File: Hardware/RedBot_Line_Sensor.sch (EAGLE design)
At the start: 9 parts, among them U1 QRE1113

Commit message: Change to Rev 10 for release  - flipped connector to bottom side of board  - change revision number
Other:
- note added: "10"
- note removed: "v01"
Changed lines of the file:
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@@
 <plain>
 <text x="172.72" y="7.62" size="3.81" layer="94">M. Hord</text>
-<text x="237.49" y="6.604" size="3.81" layer="94">v01</text>
+<text x="237.49" y="6.604" size="3.81" layer="94">10</text>
 </plain>
 <instances>

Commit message: Production Readied
Added fiducial reference points & created panel for manufacture.
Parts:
- added FID1, FID2: FIDUCIALUFIDUCIAL, SparkFun-Aesthetics:FIDUCIALUFIDUCIAL
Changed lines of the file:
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@@
 <part name="STANDOFF1" library="SparkFun-Electromechanical" deviceset="STAND-OFF" device=""/>
 <part name="LOGO3" library="SparkFun-Aesthetics" deviceset="LOGO-SFE" device="SK"/>
+<part name="FID1" library="SparkFun-Aesthetics" deviceset="FIDUCIAL" device="UFIDUCIAL"/>
+<part name="FID2" library="SparkFun-Aesthetics" deviceset="FIDUCIAL" device="UFIDUCIAL"/>
 </parts>
 <sheets>
@@
 <instance part="STANDOFF1" gate="G$1" x="246.38" y="33.02"/>
 <instance part="LOGO3" gate="G$1" x="241.3" y="17.78"/>
+<instance part="FID1" gate="G$1" x="241.3" y="30.48"/>
+<instance part="FID2" gate="G$1" x="241.3" y="25.4"/>
 </instances>
 <busses>

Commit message: QC Revision
Changes:
1.) 0402 to 0603 footprint
2.) Updated QRE1113 footprint
3.) New 3-pin SMD header footprint w/ bosses
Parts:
- JP1: device SparkFun-Connectors:M03SMD_RA_MALE -> SparkFun-Connectors:M03SMD_RA_MALE_POST
- R2: device SparkFun-Resistors:10KOHM1/10W1%(0603) -> SparkFun-Resistors:10KOHM1/10W1%(0603)0603
- U1: value QRE1113 -> QRE1113SMD-W; device SparkFun-Sensors:QRE1113 -> SparkFun-Sensors:QRE1113SMD-W
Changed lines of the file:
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@@
 <?xml version="1.0" encoding="utf-8"?>
 <!DOCTYPE eagle SYSTEM "eagle.dtd">
-<eagle version="6.4">
+<eagle version="6.5.0">
 <drawing>
 <settings>
@@
 <grid distance="0.1" unitdist="inch" unit="inch" style="lines" multiple="1" display="no" altdistance="0.01" altunitdist="inch" altunit="inch"/>
 <layers>
-<layer number="1" name="Top" color="4" fill="1" visible="no" active="no"/>
-<layer number="2" name="Route2" color="1" fill="3" visible="no" active="no"/>
-<layer number="3" name="Route3" color="4" fill="3" visible="no" active="no"/>
-<layer number="4" name="Route4" color="1" fill="4" visible="no" active="no"/>
-<layer number="5" name="Route5" color="4" fill="4" visible="no" active="no"/>
-<layer number="6" name="Route6" color="1" fill="8" visible="no" active="no"/>
-<layer number="7" name="Route7" color="4" fill="8" visible="no" active="no"/>
-<layer number="8" name="Route8" color="1" fill="2" visible="no" active="no"/>
-<layer number="9" name="Route9" color="4" fill="2" visible="no" active="no"/>
-<layer number="10" name="Route10" color="1" fill="7" visible="no" active="no"/>
-<layer number="11" name="Route11" color="4" fill="7" visible="no" active="no"/>
-<layer number="12" name="Route12" color="1" fill="5" visible="no" active="no"/>
-<layer number="13" name="Route13" color="4" fill="5" visible="no" active="no"/>
-<layer number="14" name="Route14" color="1" fill="6" visible="no" active="no"/>
-<layer number="15" name="Route15" color="4" fill="6" visible="no" active="no"/>
-<layer number="16" name="Bottom" color="1" fill="1" visible="no" active="no"/>
-<layer number="17" name="Pads" color="2" fill="1" visible="no" active="no"/>
-<layer number="18" name="Vias" color="2" fill="1" visible="no" active="no"/>
-<layer number="19" name="Unrouted" color="6" fill="1" visible="no" active="no"/>
-<layer number="20" name="Dimension" color="15" fill="1" visible="no" active="no"/>
-<layer number="21" name="tPlace" color="7" fill="1" visible="no" active="no"/>
-<layer number="22" name="bPlace" color="7" fill="1" visible="no" active="no"/>
-<layer number="23" name="tOrigins" color="15" fill="1" visible="no" active="no"/>
-<layer number="24" name="bOrigins" color="15" fill="1" visible="no" active="no"/>
-<layer number="25" name="tNames" color="7" fill="1" visible="no" active="no"/>
-<layer number="26" name="bNames" color="7" fill="1" visible="no" active="no"/>
-<layer number="27" name="tValues" color="7" fill="1" visible="no" active="no"/>
-<layer number="28" name="bValues" color="7" fill="1" visible="no" active="no"/>
+<layer number="1" name="Top" color="4" fill="1" visible="yes" active="no"/>
+<layer number="2" name="Route2" color="1" fill="3" visible="yes" active="no"/>
+<layer number="3" name="Route3" color="4" fill="3" visible="yes" active="no"/>
+<layer number="4" name="Route4" color="1" fill="4" visible="yes" active="no"/>
+<layer number="5" name="Route5" color="4" fill="4" visible="yes" active="no"/>
+<layer number="6" name="Route6" color="1" fill="8" visible="yes" active="no"/>
+<layer number="7" name="Route7" color="4" fill="8" visible="yes" active="no"/>
+<layer number="8" name="Route8" color="1" fill="2" visible="yes" active="no"/>
+<layer number="9" name="Route9" color="4" fill="2" visible="yes" active="no"/>
+<layer number="10" name="Route10" color="1" fill="7" visible="yes" active="no"/>
+<layer number="11" name="Route11" color="4" fill="7" visible="yes" active="no"/>
+<layer number="12" name="Route12" color="1" fill="5" visible="yes" active="no"/>
+<layer number="13" name="Route13" color="4" fill="5" visible="yes" active="no"/>
+<layer number="14" name="Route14" color="1" fill="6" visible="yes" active="no"/>
+<layer number="15" name="Route15" color="4" fill="6" visible="yes" active="no"/>
+<layer number="16" name="Bottom" color="1" fill="1" visible="yes" active="no"/>
+<layer number="17" name="Pads" color="2" fill="1" visible="yes" active="no"/>
+<layer number="18" name="Vias" color="2" fill="1" visible="yes" active="no"/>
+<layer number="19" name="Unrouted" color="6" fill="1" visible="yes" active="no"/>
+<layer number="20" name="Dimension" color="6" fill="1" visible="yes" active="no"/>
+<layer number="21" name="tPlace" color="16" fill="1" visible="yes" active="no"/>
+<layer number="22" name="bPlace" color="14" fill="1" visible="yes" active="no"/>
+<layer number="23" name="tOrigins" color="15" fill="1" visible="yes" active="no"/>
+<layer number="24" name="bOrigins" color="15" fill="1" visible="yes" active="no"/>
+<layer number="25" name="tNames" color="7" fill="1" visible="yes" active="no"/>
+<layer number="26" name="bNames" color="7" fill="1" visible="yes" active="no"/>
+<layer number="27" name="tValues" color="7" fill="1" visible="yes" active="no"/>
+<layer number="28" name="bValues" color="7" fill="1" visible="yes" active="no"/>
 <layer number="29" name="tStop" color="7" fill="3" visible="no" active="no"/>
 <layer number="30" name="bStop" color="7" fill="6" visible="no" active="no"/>
@@
 <layer number="35" name="tGlue" color="7" fill="4" visible="no" active="no"/>
 <layer number="36" name="bGlue" color="7" fill="5" visible="no" active="no"/>
-<layer number="37" name="tTest" color="7" fill="1" visible="no" active="no"/>
-<layer number="38" name="bTest" color="7" fill="1" visible="no" active="no"/>
+<layer number="37" name="tTest" color="7" fill="1" visible="yes" active="no"/>
+<layer number="38" name="bTest" color="7" fill="1" visible="yes" active="no"/>
 <layer number="39" name="tKeepout" color="4" fill="11" visible="no" active="no"/>
 <layer number="40" name="bKeepout" color="1" fill="11" visible="no" active="no"/>
@@
 <layer number="44" name="Drills" color="7" fill="1" visible="no" active="no"/>
 <layer number="45" name="Holes" color="7" fill="1" visible="no" active="no"/>
-<layer number="46" name="Milling" color="3" fill="1" visible="no" active="no"/>
-<layer number="47" name="Measures" color="7" fill="1" visible="no" active="no"/>
-<layer number="48" name="Document" color="7" fill="1" visible="no" active="no"/>
-<layer number="49" name="Reference" color="7" fill="1" visible="no" active="no"/>
-<layer number="50" name="dxf" color="7" fill="1" visible="no" active="no"/>
-<layer number="51" name="tDocu" color="7" fill="1" visible="no" active="no"/>
-<layer number="52" name="bDocu" color="7" fill="1" visible="no" active="no"/>
-<layer number="53" name="tGND_GNDA" color="7" fill="9" visible="no" active="no"/>
-<layer number="54" name="bGND_GNDA" color="1" fill="9" visible="no" active="no"/>
-<layer number="56" name="wert" color="7" fill="1" visible="no" active="no"/>
+<layer number="46" name="Milling" color="3" fill="1" visible="yes" active="no"/>
+<layer number="47" name="Measures" color="7" fill="1" visible="yes" active="no"/>
+<layer number="48" name="Document" color="7" fill="1" visible="yes" active="no"/>
+<layer number="49" name="Reference" color="7" fill="1" visible="yes" active="no"/>
+<layer number="50" name="dxf" color="7" fill="1" visible="yes" active="no"/>
+<layer number="51" name="tDocu" color="6" fill="1" visible="yes" active="no"/>
+<layer number="52" name="bDocu" color="7" fill="1" visible="yes" active="no"/>
+<layer number="53" name="tGND_GNDA" color="7" fill="9" visible="yes" active="no"/>
+<layer number="54" name="bGND_GNDA" color="1" fill="9" visible="yes" active="no"/>
+<layer number="56" name="wert" color="7" fill="1" visible="yes" active="no"/>
 <layer number="91" name="Nets" color="2" fill="1" visible="yes" active="yes"/>
 <layer number="92" name="Busses" color="1" fill="1" visible="yes" active="yes"/>
@@
 <layer number="106" name="bPlate" color="7" fill="1" visible="no" active="yes"/>
 <layer number="107" name="Crop" color="7" fill="1" visible="no" active="yes"/>
+<layer number="108" name="tplace-old" color="10" fill="1" visible="yes" active="yes"/>
+<layer number="109" name="ref-old" color="11" fill="1" visible="yes" active="yes"/>
 <layer number="116" name="Patch_BOT" color="9" fill="4" visible="no" active="yes"/>
 <layer number="121" name="_tsilk" color="7" fill="1" visible="no" active="yes"/>
@@
 <part name="LOGO1" library="SparkFun-Aesthetics" deviceset="LOGO-SFE" device="SK"/>
 <part name="LOGO2" library="SparkFun-Aesthetics" deviceset="OSHW-LOGO" device="S"/>
-<part name="U1" library="SparkFun-Sensors" deviceset="QRE1113" device=""/>
+<part name="U1" library="SparkFun-Sensors" deviceset="QRE1113" device="SMD-W" value="QRE1113SMD-W"/>
 <part name="R1" library="SparkFun-Resistors" deviceset="100-1%" device="" value="100"/>
-<part name="R2" library="SparkFun-Resistors" deviceset="10KOHM1/10W1%(0603)" device="" value="10k"/>
-<part name="JP1" library="SparkFun-Connectors" deviceset="M03" device="SMD_RA_MALE"/>
+<part name="R2" library="SparkFun-Resistors" deviceset="10KOHM1/10W1%(0603)" device="0603" value="10k"/>
+<part name="JP1" library="SparkFun-Connectors" deviceset="M03" device="SMD_RA_MALE_POST"/>
 <part name="STANDOFF1" library="SparkFun-Electromechanical" deviceset="STAND-OFF" device=""/>
 <part name="LOGO3" library="SparkFun-Aesthetics" deviceset="LOGO-SFE" device="SK"/>

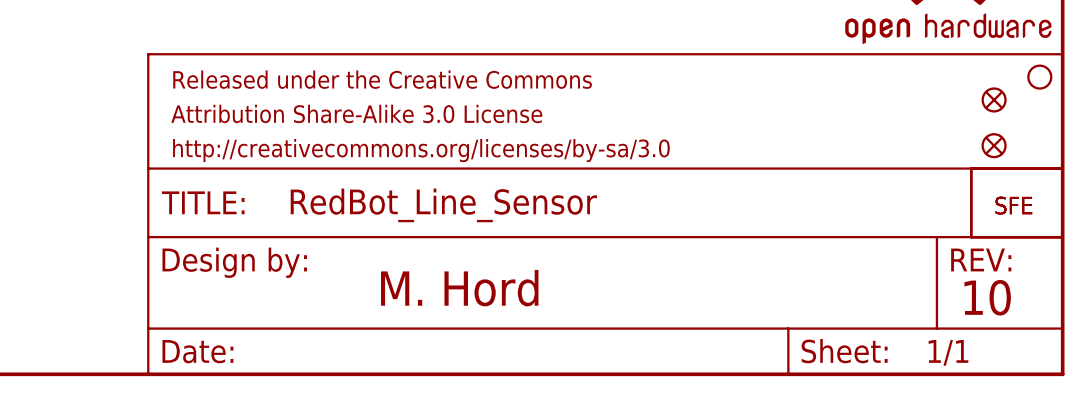
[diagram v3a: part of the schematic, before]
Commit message: Minor aesthetic fixes
1.) Moved VCC via away from silk
2.) Moved board name silk away from header boss holes
3.) Updated version info in schematic.
4.) Moved flame on top side out to avoid resistor tcreme.
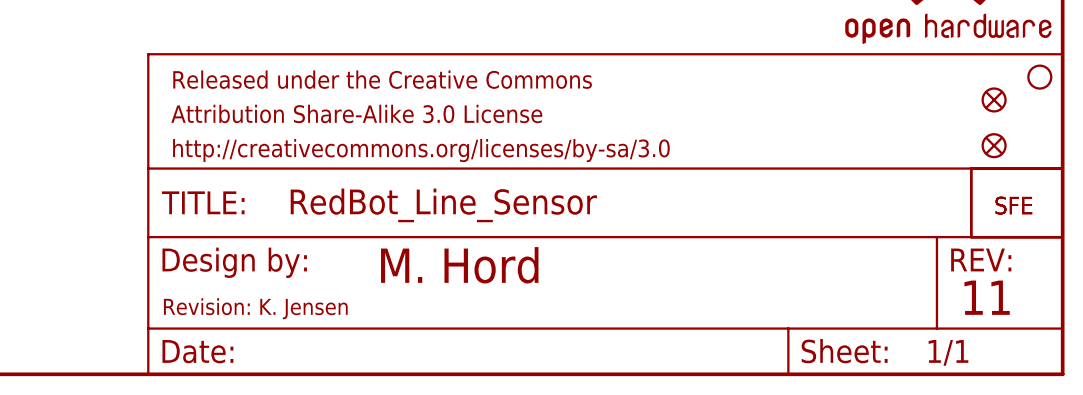
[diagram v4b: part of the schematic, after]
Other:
- note added: "11"
- note added: "Revision: K. Jensen"
- note removed: "10"
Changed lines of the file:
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@@
 <?xml version="1.0" encoding="utf-8"?>
 <!DOCTYPE eagle SYSTEM "eagle.dtd">
-<eagle version="6.5.0">
+<eagle version="6.4">
 <drawing>
 <settings>
@@
 <grid distance="0.1" unitdist="inch" unit="inch" style="lines" multiple="1" display="no" altdistance="0.01" altunitdist="inch" altunit="inch"/>
 <layers>
-<layer number="1" name="Top" color="4" fill="1" visible="yes" active="no"/>
-<layer number="2" name="Route2" color="1" fill="3" visible="yes" active="no"/>
-<layer number="3" name="Route3" color="4" fill="3" visible="yes" active="no"/>
-<layer number="4" name="Route4" color="1" fill="4" visible="yes" active="no"/>
-<layer number="5" name="Route5" color="4" fill="4" visible="yes" active="no"/>
-<layer number="6" name="Route6" color="1" fill="8" visible="yes" active="no"/>
-<layer number="7" name="Route7" color="4" fill="8" visible="yes" active="no"/>
-<layer number="8" name="Route8" color="1" fill="2" visible="yes" active="no"/>
-<layer number="9" name="Route9" color="4" fill="2" visible="yes" active="no"/>
-<layer number="10" name="Route10" color="1" fill="7" visible="yes" active="no"/>
-<layer number="11" name="Route11" color="4" fill="7" visible="yes" active="no"/>
-<layer number="12" name="Route12" color="1" fill="5" visible="yes" active="no"/>
-<layer number="13" name="Route13" color="4" fill="5" visible="yes" active="no"/>
-<layer number="14" name="Route14" color="1" fill="6" visible="yes" active="no"/>
-<layer number="15" name="Route15" color="4" fill="6" visible="yes" active="no"/>
-<layer number="16" name="Bottom" color="1" fill="1" visible="yes" active="no"/>
-<layer number="17" name="Pads" color="2" fill="1" visible="yes" active="no"/>
-<layer number="18" name="Vias" color="2" fill="1" visible="yes" active="no"/>
-<layer number="19" name="Unrouted" color="6" fill="1" visible="yes" active="no"/>
-<layer number="20" name="Dimension" color="6" fill="1" visible="yes" active="no"/>
-<layer number="21" name="tPlace" color="16" fill="1" visible="yes" active="no"/>
-<layer number="22" name="bPlace" color="14" fill="1" visible="yes" active="no"/>
-<layer number="23" name="tOrigins" color="15" fill="1" visible="yes" active="no"/>
-<layer number="24" name="bOrigins" color="15" fill="1" visible="yes" active="no"/>
-<layer number="25" name="tNames" color="7" fill="1" visible="yes" active="no"/>
-<layer number="26" name="bNames" color="7" fill="1" visible="yes" active="no"/>
-<layer number="27" name="tValues" color="7" fill="1" visible="yes" active="no"/>
-<layer number="28" name="bValues" color="7" fill="1" visible="yes" active="no"/>
+<layer number="1" name="Top" color="4" fill="1" visible="no" active="no"/>
+<layer number="2" name="Route2" color="1" fill="3" visible="no" active="no"/>
+<layer number="3" name="Route3" color="4" fill="3" visible="no" active="no"/>
+<layer number="4" name="Route4" color="1" fill="4" visible="no" active="no"/>
+<layer number="5" name="Route5" color="4" fill="4" visible="no" active="no"/>
+<layer number="6" name="Route6" color="1" fill="8" visible="no" active="no"/>
+<layer number="7" name="Route7" color="4" fill="8" visible="no" active="no"/>
+<layer number="8" name="Route8" color="1" fill="2" visible="no" active="no"/>
+<layer number="9" name="Route9" color="4" fill="2" visible="no" active="no"/>
+<layer number="10" name="Route10" color="1" fill="7" visible="no" active="no"/>
+<layer number="11" name="Route11" color="4" fill="7" visible="no" active="no"/>
+<layer number="12" name="Route12" color="1" fill="5" visible="no" active="no"/>
+<layer number="13" name="Route13" color="4" fill="5" visible="no" active="no"/>
+<layer number="14" name="Route14" color="1" fill="6" visible="no" active="no"/>
+<layer number="15" name="Route15" color="4" fill="6" visible="no" active="no"/>
+<layer number="16" name="Bottom" color="1" fill="1" visible="no" active="no"/>
+<layer number="17" name="Pads" color="2" fill="1" visible="no" active="no"/>
+<layer number="18" name="Vias" color="2" fill="1" visible="no" active="no"/>
+<layer number="19" name="Unrouted" color="6" fill="1" visible="no" active="no"/>
+<layer number="20" name="Dimension" color="6" fill="1" visible="no" active="no"/>
+<layer number="21" name="tPlace" color="16" fill="1" visible="no" active="no"/>
+<layer number="22" name="bPlace" color="14" fill="1" visible="no" active="no"/>
+<layer number="23" name="tOrigins" color="15" fill="1" visible="no" active="no"/>
+<layer number="24" name="bOrigins" color="15" fill="1" visible="no" active="no"/>
+<layer number="25" name="tNames" color="7" fill="1" visible="no" active="no"/>
+<layer number="26" name="bNames" color="7" fill="1" visible="no" active="no"/>
+<layer number="27" name="tValues" color="7" fill="1" visible="no" active="no"/>
+<layer number="28" name="bValues" color="7" fill="1" visible="no" active="no"/>
 <layer number="29" name="tStop" color="7" fill="3" visible="no" active="no"/>
 <layer number="30" name="bStop" color="7" fill="6" visible="no" active="no"/>
@@
 <layer number="35" name="tGlue" color="7" fill="4" visible="no" active="no"/>
 <layer number="36" name="bGlue" color="7" fill="5" visible="no" active="no"/>
-<layer number="37" name="tTest" color="7" fill="1" visible="yes" active="no"/>
-<layer number="38" name="bTest" color="7" fill="1" visible="yes" active="no"/>
+<layer number="37" name="tTest" color="7" fill="1" visible="no" active="no"/>
+<layer number="38" name="bTest" color="7" fill="1" visible="no" active="no"/>
 <layer number="39" name="tKeepout" color="4" fill="11" visible="no" active="no"/>
 <layer number="40" name="bKeepout" color="1" fill="11" visible="no" active="no"/>
@@
 <layer number="44" name="Drills" color="7" fill="1" visible="no" active="no"/>
 <layer number="45" name="Holes" color="7" fill="1" visible="no" active="no"/>
-<layer number="46" name="Milling" color="3" fill="1" visible="yes" active="no"/>
-<layer number="47" name="Measures" color="7" fill="1" visible="yes" active="no"/>
-<layer number="48" name="Document" color="7" fill="1" visible="yes" active="no"/>
-<layer number="49" name="Reference" color="7" fill="1" visible="yes" active="no"/>
-<layer number="50" name="dxf" color="7" fill="1" visible="yes" active="no"/>
-<layer number="51" name="tDocu" color="6" fill="1" visible="yes" active="no"/>
-<layer number="52" name="bDocu" color="7" fill="1" visible="yes" active="no"/>
-<layer number="53" name="tGND_GNDA" color="7" fill="9" visible="yes" active="no"/>
-<layer number="54" name="bGND_GNDA" color="1" fill="9" visible="yes" active="no"/>
-<layer number="56" name="wert" color="7" fill="1" visible="yes" active="no"/>
+<layer number="46" name="Milling" color="3" fill="1" visible="no" active="no"/>
+<layer number="47" name="Measures" color="7" fill="1" visible="no" active="no"/>
+<layer number="48" name="Document" color="7" fill="1" visible="no" active="no"/>
+<layer number="49" name="Reference" color="7" fill="1" visible="no" active="no"/>
+<layer number="50" name="dxf" color="7" fill="1" visible="no" active="no"/>
+<layer number="51" name="tDocu" color="6" fill="1" visible="no" active="no"/>
+<layer number="52" name="bDocu" color="7" fill="1" visible="no" active="no"/>
+<layer number="53" name="tGND_GNDA" color="7" fill="9" visible="no" active="no"/>
+<layer number="54" name="bGND_GNDA" color="1" fill="9" visible="no" active="no"/>
+<layer number="56" name="wert" color="7" fill="1" visible="no" active="no"/>
 <layer number="91" name="Nets" color="2" fill="1" visible="yes" active="yes"/>
 <layer number="92" name="Busses" color="1" fill="1" visible="yes" active="yes"/>
@@
 <sheet>
 <plain>
-<text x="172.72" y="7.62" size="3.81" layer="94">M. Hord</text>
-<text x="237.49" y="6.604" size="3.81" layer="94">10</text>
+<text x="172.72" y="10.16" size="3.81" layer="94">M. Hord</text>
+<text x="237.49" y="6.604" size="3.81" layer="94">11</text>
+<text x="148.844" y="6.604" size="1.778" layer="94">Revision: K. Jensen</text>
 </plain>
 <instances>

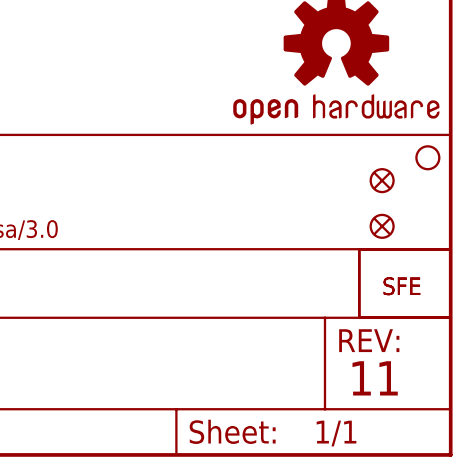
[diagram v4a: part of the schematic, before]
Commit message: Silk fixes and trace reroutes
Fixed top silk so pin labels are closer to edge of board and nothing
gets cut off. Removed flame from top. Cleaned up "out" and "vcc" traces
to be more efficient.
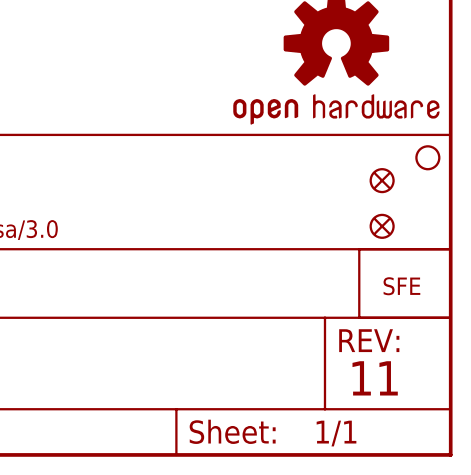
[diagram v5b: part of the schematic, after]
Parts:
- removed LOGO1: LOGO-SFESK, SparkFun-Aesthetics:LOGO-SFESK
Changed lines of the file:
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@@
 <?xml version="1.0" encoding="utf-8"?>
 <!DOCTYPE eagle SYSTEM "eagle.dtd">
-<eagle version="6.4">
+<eagle version="6.5.0">
 <drawing>
 <settings>
@@
 <part name="SUPPLY1" library="SparkFun-Aesthetics" deviceset="5V" device=""/>
 <part name="GND1" library="SparkFun-Aesthetics" deviceset="GND" device=""/>
-<part name="LOGO1" library="SparkFun-Aesthetics" deviceset="LOGO-SFE" device="SK"/>
 <part name="LOGO2" library="SparkFun-Aesthetics" deviceset="OSHW-LOGO" device="S"/>
 <part name="U1" library="SparkFun-Sensors" deviceset="QRE1113" device="SMD-W" value="QRE1113SMD-W"/>
@@
 <instance part="SUPPLY1" gate="G$1" x="124.46" y="121.92"/>
 <instance part="GND1" gate="1" x="124.46" y="81.28"/>
-<instance part="LOGO1" gate="G$1" x="241.3" y="17.78"/>
 <instance part="LOGO2" gate="G$1" x="236.22" y="45.72"/>
 <instance part="U1" gate="G$1" x="137.16" y="96.52" smashed="yes">
